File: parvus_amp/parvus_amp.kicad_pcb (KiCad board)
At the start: 2 copper layers, 86 x 60 mm, 40 parts, among them J1 input, J2 output, J3 powersupply, U1 LM3886

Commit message: Updated schematic and README description
Signed-off-by: Nenad Radulovic <nenad.b.radulovic@gmail.com>
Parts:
- added C15: 100n, Capacitor_THT:C_Rect_L7.0mm_W3.5mm_P5.00mm, F.Cu at (152.6, 100.3)
- added D1: BZX85C16, Diode_THT:D_DO-35_SOD27_P7.62mm_Horizontal, F.Cu at (94.9, 65.4)
- added R14: 10, Resistor_THT:R_Axial_DIN0207_L6.3mm_D2.5mm_P10.16mm_Horizontal, F.Cu at (148.2, 110.5)
- R11: renamed from R13; value 100k -> 7k5
- renumbered C9 to C1, C6 to C10, C1 to C11, C7 to C12, C8 to C13, C2 to C14, C12 to C2, C4 to C3, C10 to C4, C13 to C5, C5 to C6, C11 to C7, C14 to C8, C3 to C9, D1 to D2, D2 to D3, J3 to J1, J1 to J2, J2 to J3, MK3 to MK2, MK2 to MK3, R11 to R1, R12 to R10, R2 to R12, R8 to R13, R3 to R2, R4 to R3, R7 to R4, R9 to R6, R1 to R7, R6 to R8, R10 to R9
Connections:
- C13 pad 2: Net-(C8-Pad2) -> Net-(C13-Pad2)
- R11 pad 1: Net-(C8-Pad2) -> Net-(C13-Pad2)
- U1 pad 8: Net-(C8-Pad2) -> Net-(D1-Pad1)

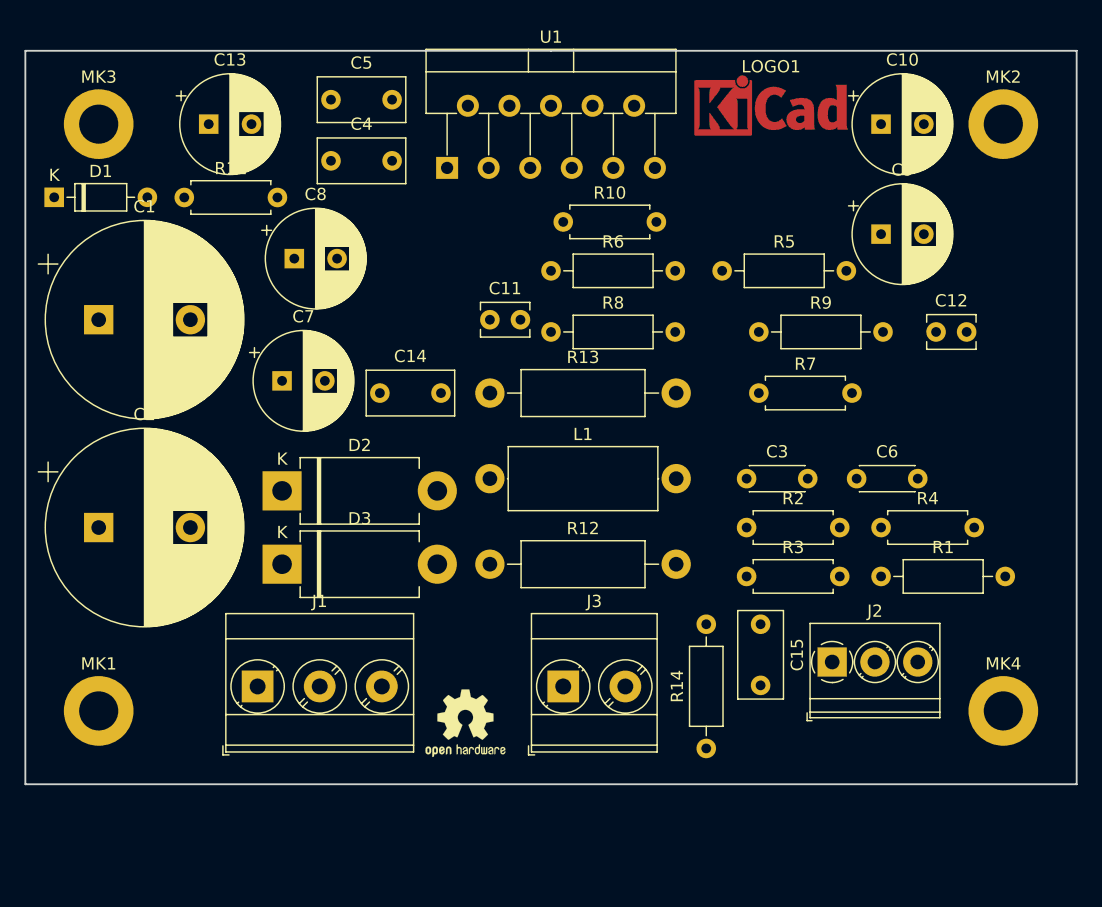
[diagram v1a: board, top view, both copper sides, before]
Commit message: Using Phoenix MCV type of connectors
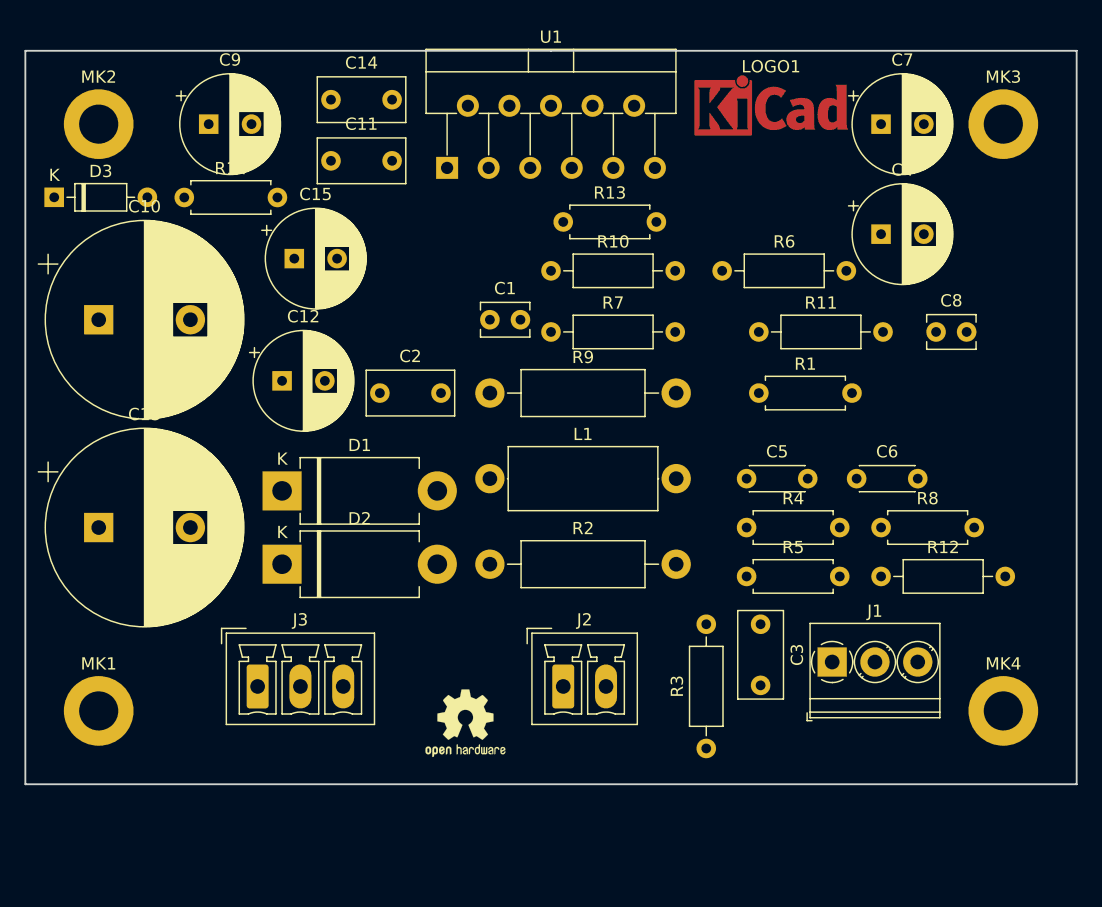
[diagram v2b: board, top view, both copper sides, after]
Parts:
- removed the J1 at (111.5, 105.4)
- added J2: output, Connector_Phoenix_MC:PhoenixContact_MCV_1,5_2-G-3.5_1x02_P3.50mm_Vertical, F.Cu at (136.5, 105.4)
- J3: value output -> powersupply; footprint TerminalBlock_Phoenix:TerminalBlock_Phoenix_MKDS-3-2-5.08_1x02_P5.08mm_Horizontal -> Connector_Phoenix_MC:PhoenixContact_MCV_1,5_3-G-3.5_1x03_P3.50mm_Vertical
- moved J3 25.0 mm to (111.5, 105.4)
- renumbered C11 to C1, C1 to C10, C4 to C11, C7 to C12, C2 to C13, C5 to C14, C8 to C15, C14 to C2, C15 to C3, C9 to C4, C3 to C5, C10 to C7, C12 to C8, C13 to C9, D2 to D1, D3 to D2, D1 to D3, J2 to J1, MK3 to MK2, MK2 to MK3, R7 to R1, R6 to R10, R9 to R11, R1 to R12, R10 to R13, R11 to R14, R12 to R2, R14 to R3, R2 to R4, R3 to R5, R5 to R6, R8 to R7, R4 to R8, R13 to R9
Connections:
- C3 pad 2: Net-(C15-Pad2) -> Net-(C3-Pad2)
- C4 pad 2: Net-(C6-Pad1) -> Net-(C4-Pad2)
- C6 pad 1: Net-(C6-Pad1) -> Net-(C4-Pad2)
- J1 pad 1: Net-(J2-Pad1) -> Net-(J1-Pad1)
- J3 pad 1: GNDPWR -> VCC
- J3 pad 2: Net-(C15-Pad2) -> GNDPWR
- L1 pad 2: Net-(C15-Pad2) -> Net-(C3-Pad2)
- R4 pad 2: Net-(J2-Pad1) -> Net-(J1-Pad1)
- R5 pad 1: Net-(C6-Pad1) -> Net-(C4-Pad2)
- R8 pad 1: Net-(C6-Pad1) -> Net-(J1-Pad1)
- R9 pad 1: Net-(C15-Pad2) -> Net-(C3-Pad2)

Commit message: Finished the amp board.
Signed-off-by: Nenad Radulovic <nenad.b.radulovic@gmail.com>
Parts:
- removed C13: 2m2, Capacitor_THT:CP_Radial_D16.0mm_P7.50mm
- removed C14: 100n, Capacitor_THT:C_Rect_L7.0mm_W3.5mm_P5.00mm
- removed C15: 100u, Capacitor_THT:CP_Radial_D8.0mm_P3.50mm
- removed R10: 499, Resistor_THT:R_Axial_DIN0207_L6.3mm_D2.5mm_P10.16mm_Horizontal
- removed R11: 7k5, Resistor_THT:R_Axial_DIN0207_L6.3mm_D2.5mm_P10.16mm_Horizontal
- removed R12: 10, Resistor_THT:R_Axial_DIN0207_L6.3mm_D2.5mm_P10.16mm_Horizontal
- removed R13: 1k6, Resistor_THT:R_Axial_DIN0207_L6.3mm_D2.5mm_P7.62mm_Horizontal
- removed R14: 7k5, Resistor_THT:R_Axial_DIN0207_L6.3mm_D2.5mm_P7.62mm_Horizontal
- added Cf1: 68p, Capacitor_THT:C_Disc_D3.8mm_W2.6mm_P2.50mm, F.Cu at (140.6, 76.8)
- added Ci1: 2m2, Capacitor_THT:CP_Radial_D10.0mm_P3.50mm, F.Cu at (156.1, 63.5)
- added Rf1: 1k5, Resistor_THT:R_Axial_DIN0411_L9.9mm_D3.6mm_P12.70mm_Horizontal, F.Cu at (130.4, 67.3)
- added Rf2: 430, Resistor_THT:R_Axial_DIN0207_L6.3mm_D2.5mm_P10.16mm_Horizontal, F.Cu at (140.6, 72.4)
- added Ri1: 100, Resistor_THT:R_Axial_DIN0207_L6.3mm_D2.5mm_P10.16mm_Horizontal, F.Cu at (149.5, 71.1)
- C1: value 15p -> 2m2; footprint Capacitor_THT:C_Disc_D3.8mm_W2.6mm_P2.50mm -> Capacitor_THT:CP_Radial_D16.0mm_P7.50mm
- C10: value 2m2 -> 100u; footprint Capacitor_THT:CP_Radial_D16.0mm_P7.50mm -> Capacitor_THT:CP_Radial_D8.0mm_P3.50mm
- C11: value 100n -> 220n
- C12, C9: value 100u -> 100n; footprint Capacitor_THT:CP_Radial_D8.0mm_P3.50mm -> Capacitor_THT:C_Rect_L7.0mm_W3.5mm_P5.00mm
- C2: value 220n -> 2m2; footprint Capacitor_THT:C_Rect_L7.0mm_W3.5mm_P5.00mm -> Capacitor_THT:CP_Radial_D16.0mm_P7.50mm
- C3: value 100n -> 100u; footprint Capacitor_THT:C_Rect_L7.0mm_W3.5mm_P5.00mm -> Capacitor_THT:CP_Radial_D8.0mm_P3.50mm
- C4: value 470u -> 100u
- C5: value 220p -> 100u; footprint Capacitor_THT:C_Disc_D4.3mm_W1.9mm_P5.00mm -> Capacitor_THT:CP_Radial_D8.0mm_P3.50mm
- C6: value 1n -> 2n2; footprint Capacitor_THT:C_Disc_D4.3mm_W1.9mm_P5.00mm -> Capacitor_THT:C_Disc_D5.1mm_W3.2mm_P5.00mm
- C7: value 470u -> 2n2; footprint Capacitor_THT:CP_Radial_D8.0mm_P3.50mm -> Capacitor_THT:C_Disc_D5.1mm_W3.2mm_P5.00mm
- C8: value 15p -> 100n; footprint Capacitor_THT:C_Disc_D3.8mm_W2.6mm_P2.50mm -> Capacitor_THT:C_Rect_L7.0mm_W3.5mm_P5.00mm
- D1: value 1N5404 -> BZX85C16; footprint Diode_THT:D_DO-201AD_P12.70mm_Horizontal -> Diode_THT:D_DO-35_SOD27_P10.16mm_Horizontal
- D3: value BZX85C16 -> 1N5404; footprint Diode_THT:D_DO-35_SOD27_P7.62mm_Horizontal -> Diode_THT:D_DO-201AD_P12.70mm_Horizontal
- J1: value input -> powersupply; footprint TerminalBlock_Phoenix:TerminalBlock_Phoenix_PT-1,5-3-3.5-H_1x03_P3.50mm_Horizontal -> Connector_Phoenix_MC:PhoenixContact_MCV_1,5_4-G-3.5_1x04_P3.50mm_Vertical
- J2: value output -> input; footprint Connector_Phoenix_MC:PhoenixContact_MCV_1,5_2-G-3.5_1x02_P3.50mm_Vertical -> TerminalBlock_Phoenix:TerminalBlock_Phoenix_PT-1,5-3-3.5-H_1x03_P3.50mm_Horizontal
- J3: value powersupply -> output; footprint Connector_Phoenix_MC:PhoenixContact_MCV_1,5_3-G-3.5_1x03_P3.50mm_Vertical -> Connector_Phoenix_MC:PhoenixContact_MCV_1,5_2-G-3.5_1x02_P3.50mm_Vertical
- L1: footprint Inductor_THT:L_Axial_L12.0mm_D5.0mm_P15.24mm_Horizontal_Fastron_MISC -> Inductor_THT:L_Axial_L9.5mm_D4.0mm_P12.70mm_Horizontal_Fastron_SMCC
- LOGO1: moved to B.Cu
- R1: value 1k6 -> 10; footprint Resistor_THT:R_Axial_DIN0207_L6.3mm_D2.5mm_P7.62mm_Horizontal -> Resistor_THT:R_Axial_DIN0207_L6.3mm_D2.5mm_P10.16mm_Horizontal
- R2: value 4.7 -> 100k; footprint Resistor_THT:R_Axial_DIN0411_L9.9mm_D3.6mm_P15.24mm_Horizontal -> Resistor_THT:R_Axial_DIN0207_L6.3mm_D2.5mm_P10.16mm_Horizontal
- R3: value 10 -> 100
- R4: footprint Resistor_THT:R_Axial_DIN0207_L6.3mm_D2.5mm_P7.62mm_Horizontal -> Resistor_THT:R_Axial_DIN0207_L6.3mm_D2.5mm_P10.16mm_Horizontal
- R5: value 100 -> 1k5; footprint Resistor_THT:R_Axial_DIN0207_L6.3mm_D2.5mm_P7.62mm_Horizontal -> Resistor_THT:R_Axial_DIN0207_L6.3mm_D2.5mm_P10.16mm_Horizontal
- R6: value 499 -> 7k5
- R7: value 7k5 -> 4.7; footprint Resistor_THT:R_Axial_DIN0207_L6.3mm_D2.5mm_P10.16mm_Horizontal -> Resistor_THT:R_Axial_DIN0411_L9.9mm_D3.6mm_P12.70mm_Horizontal
- R8: value 100k -> 4.7; footprint Resistor_THT:R_Axial_DIN0207_L6.3mm_D2.5mm_P7.62mm_Horizontal -> Resistor_THT:R_Axial_DIN0411_L9.9mm_D3.6mm_P12.70mm_Horizontal
- R9: value 4.7 -> 10; footprint Resistor_THT:R_Axial_DIN0411_L9.9mm_D3.6mm_P15.24mm_Horizontal -> Resistor_THT:R_Axial_DIN0207_L6.3mm_D2.5mm_P10.16mm_Horizontal
- moved C10 68.6 mm to (163.4, 97.5), turned to 90 degrees
- moved D1 53.2 mm to (163.4, 71.1), turned to 270 degrees
- moved C4 46.7 mm to (115.8, 68.6), turned to 90 degrees
- moved D3 46.3 mm to (135.5, 87.6), turned to 180 degrees
- moved C5 45.7 mm to (115.8, 59.9), turned to 90 degrees
- moved C8 44.9 mm to (122.8, 68.6), turned to 90 degrees
- moved J1 44.9 mm to (115.0, 114.4)
- moved C12 42.3 mm to (141.2, 112.4), turned to 90 degrees
- moved R8 41.2 mm to (122.8, 103.5)
- moved LOGO1 31.1 mm to (142.2, 87.4), turned to 270 degrees
- moved R9 26.5 mm to (135.5, 107.4), turned to 180 degrees
- moved C1 25.7 mm to (115.8, 96.5), turned to 180 degrees
- moved R1 24.4 mm to (159.6, 104.8), turned to 180 degrees
- moved R3 23.9 mm to (159.6, 89.5), turned to 180 degrees
- moved R5 23.6 mm to (159.6, 74.3), turned to 180 degrees
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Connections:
- C1 pad 1: Net-(C1-Pad1) -> VCC
- C1 pad 2: Net-(C1-Pad2) -> GNDPWR
- C10 pad 1: VCC -> GNDPWR
- C10 pad 2: GNDPWR -> Net-(C10-Pad2)
- C11 pad 1: VCC -> GNDPWR
- C11 pad 2: GNDPWR -> Net-(C11-Pad2)
- C12 pad 1: VCC -> GNDPWR
- C12 pad 2: GNDPWR -> Net-(C12-Pad2)
- C2 pad 1: Net-(C2-Pad1) -> GNDPWR
- C2 pad 2: Net-(C2-Pad2) -> VEE
- C4 pad 1: Net-(C4-Pad1) -> VCC
- C4 pad 2: Net-(C4-Pad2) -> GNDPWR
- C5 pad 1: Net-(C5-Pad1) -> GNDPWR
- C5 pad 2: Net-(C1-Pad1) -> VEE
- C6 pad 1: Net-(C4-Pad2) -> Net-(C6-Pad1)
- C6 pad 2: Net-(C1-Pad1) -> /sgnd
- C7 pad 2: Net-(C1-Pad1) -> /sgnd
- C8 pad 1: Net-(C2-Pad2) -> VCC
- C8 pad 2: Net-(C8-Pad2) -> GNDPWR
- C9 pad 2: Net-(C9-Pad2) -> VEE
- D1 pad 1: VCC -> Net-(D1-Pad1)
- D1 pad 2: Net-(C2-Pad2) -> Net-(C10-Pad2)
- D2 pad 1: Net-(C2-Pad2) -> VCC
- D2 pad 2: VEE -> /out
- D3 pad 1: Net-(D3-Pad1) -> /out
- D3 pad 2: Net-(C9-Pad2) -> VEE
- J1 pad 2: GNDPWR -> VEE
- J1 pad 3: Net-(C1-Pad1) -> GNDPWR
- J2 pad 1: GNDPWR -> Net-(C3-Pad2)
- J2 pad 2: Net-(C3-Pad2) -> GNDPWR
- J3 pad 1: VCC -> Net-(J3-Pad1)
- L1 pad 1: Net-(C2-Pad2) -> /out
- L1 pad 2: Net-(C3-Pad2) -> Net-(J3-Pad1)
- R1 pad 1: Net-(R1-Pad1) -> /sgnd
- R1 pad 2: Net-(C1-Pad2) -> GNDPWR
- R2 pad 1: GNDPWR -> Net-(C3-Pad2)
- R2 pad 2: Net-(C2-Pad1) -> /sgnd
- R3 pad 1: GNDPWR -> Net-(C6-Pad1)
- R4 pad 1: Net-(C5-Pad1) -> Net-(C7-Pad1)
- R4 pad 2: Net-(J1-Pad1) -> Net-(C6-Pad1)
- R5 pad 1: Net-(C4-Pad2) -> /sgnd
- R5 pad 2: Net-(C5-Pad1) -> Net-(C7-Pad1)
- R6 pad 1: Net-(R1-Pad1) -> Net-(C10-Pad2)
- R6 pad 2: Net-(C4-Pad1) -> Net-(J1-Pad1)
- R7 pad 1: Net-(C1-Pad1) -> Net-(C11-Pad2)
- R7 pad 2: Net-(R1-Pad1) -> /out
- R8 pad 1: Net-(J1-Pad1) -> Net-(J3-Pad1)
- R8 pad 2: Net-(C1-Pad1) -> /out
- R9 pad 1: Net-(C3-Pad2) -> Net-(C12-Pad2)
- R9 pad 2: Net-(C2-Pad2) -> Net-(J3-Pad1)
- U1 pad 10: Net-(R1-Pad1) -> Net-(C7-Pad1)
- U1 pad 3: Net-(C2-Pad2) -> /out
- U1 pad 8: Net-(D3-Pad1) -> Net-(D1-Pad1)
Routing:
- net Net-(J1-Pad1): track 0.00 -> 85.8 mm
- net /sgnd: track 0.00 -> 60.3 mm
- net GNDPWR: track 0.00 -> 60.1 mm
- net VEE: track 0.00 -> 48.6 mm
- net Net-(C7-Pad1): track 0.00 -> 38.5 mm
- net Net-(D1-Pad1): track 0.00 -> 35.7 mm
- net Net-(C10-Pad2): track 0.00 -> 24.2 mm
- net Net-(Cf1-Pad2): track 0.00 -> 23.4 mm
- net Net-(C6-Pad1): track 0.00 -> 15.5 mm
- net Net-(C3-Pad2): track 0.00 -> 15.1 mm
- net Net-(Ci1-Pad1): track 0.00 -> 9.06 mm
- net /out: track 0.00 -> 7.66 mm
- net Net-(C11-Pad2): track 0.00 -> 6.84 mm
- net Net-(C12-Pad2): track 0.00 -> 5.72 mm
- net Net-(C3-Pad1): track 0.00 -> 4.45 mm
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- added copper zone on B.Cu, net /out
- added copper zone on F.Cu, net /sgnd
- added copper zone on F.Cu, net GNDPWR
- added copper zone on F.Cu, net Net-(J3-Pad1)
- added copper zone on B.Cu, net VCC
- added copper zone on B.Cu, net VEE
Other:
- board size 86 x 60 mm -> 68 x 68 mm
- net class Default: clearance 0.2 -> 0.254; trace_width 0.25 -> 1
- rule trace_clearance: 0.2 -> 0.254
- board text added: "+/PG/-/mute"
- board text added: "190523"
- board text added: "PG/out"
- board text added: "REAL-TIME CONSULTING"
- board text added: "SG/PG/in"
- board text added: "input"
- board text added: "output"
- board text added: "parvus v1.0"
- board text added: "power"
